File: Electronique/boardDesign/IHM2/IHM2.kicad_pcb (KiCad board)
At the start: 2 copper layers, 12 x 12 mm, 14 parts, among them J1 Conn_01x14, SW1 SW_Push_Dual_INIT, SW2 SW_Push_Dual_START, SW3 SW_Push_Dual_PAUSE, SW4 RotaryEncoder_Switch, U1 ER_OLEDM0.91_1x-I2C

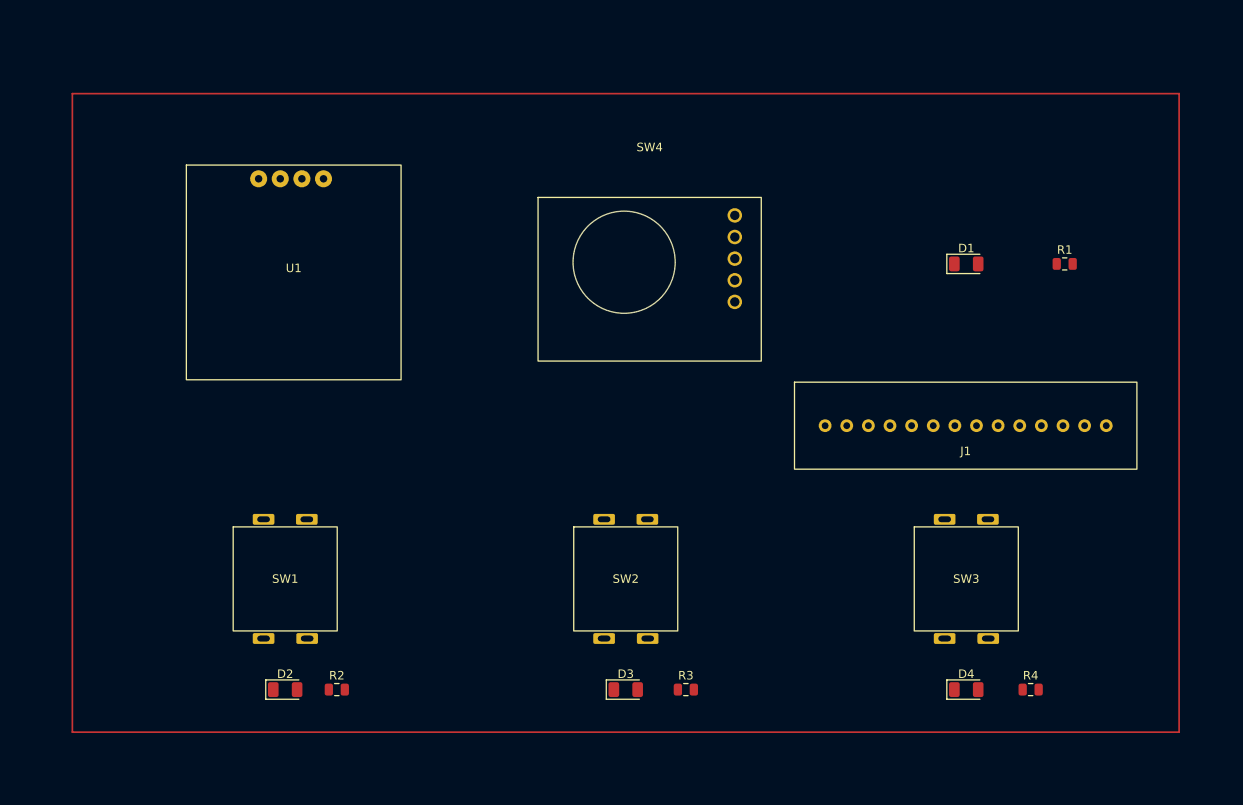
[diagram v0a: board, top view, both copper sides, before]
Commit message: feat : creation of PCB HMI with corresponding schematics and footprints doc : created links list for online resources
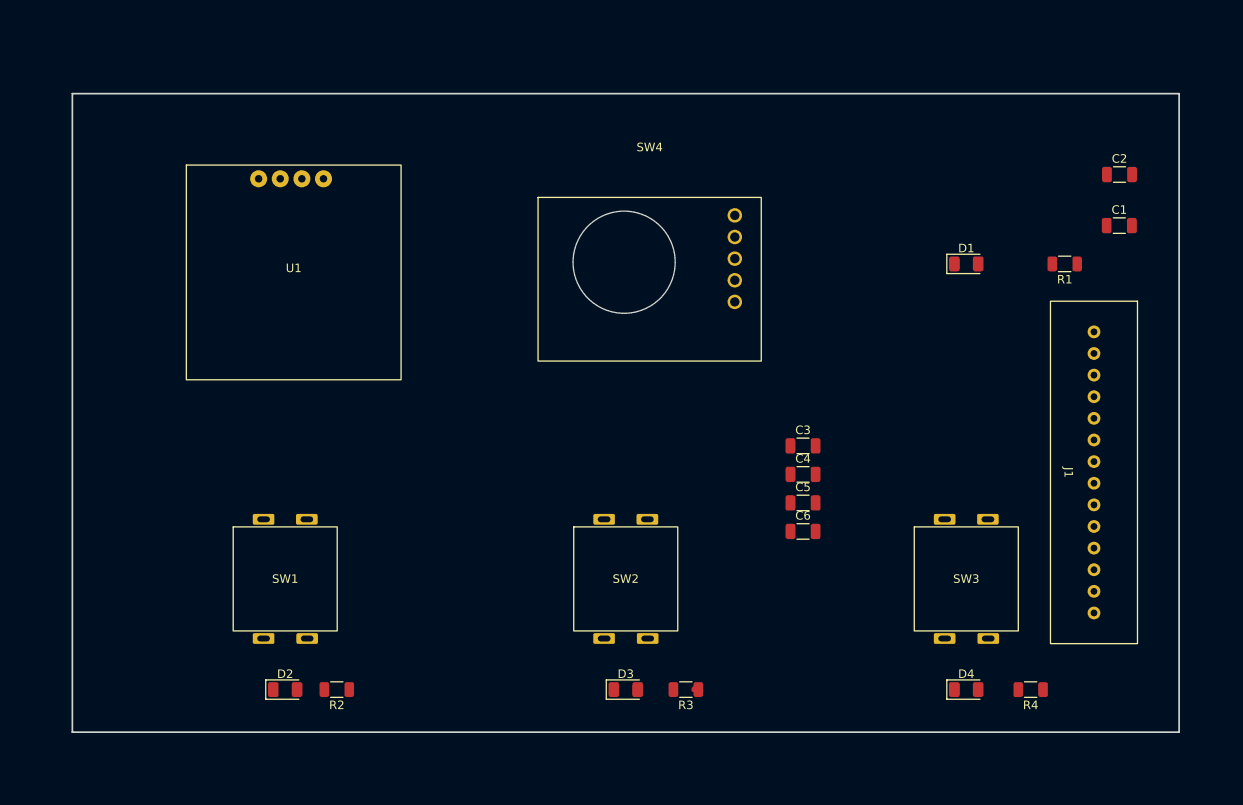
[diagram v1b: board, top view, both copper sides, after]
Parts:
- added C1: 1uF, Capacitor_SMD:C_1206_3216Metric, F.Cu at (188.5, 72.0)
- added C2: 100nF, Capacitor_SMD:C_1206_3216Metric, F.Cu at (188.5, 66.0)
- added C3: 100nF, Capacitor_SMD:C_1206_3216Metric, F.Cu at (151.3, 97.9)
- added C4: 33nF, Capacitor_SMD:C_1206_3216Metric, F.Cu at (151.3, 101.2)
- added C5: 33nF, Capacitor_SMD:C_1206_3216Metric, F.Cu at (151.3, 104.6)
- added C6: 100nF, Capacitor_SMD:C_1206_3216Metric, F.Cu at (151.3, 107.9)
- R1, R2, R3, R4: footprint PCM_4ms_Resistor:R_0805_2012Metric -> Resistor_SMD:R_1206_3216Metric
- moved J1 16.0 mm to (185.5, 101.0), turned to -90 degrees
- turned R1 to 180 degrees
- turned R2 to 180 degrees
- turned R3 to 180 degrees
- turned R4 to 180 degrees
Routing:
- net /LED_START: track 0.00 -> 0.71 mm
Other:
- board size 12 x 12 mm -> 130 x 75 mm

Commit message: fix : added capacitors for power supply and I2C component refactor : removed via rollback : wrong IHM2 version (1 GND layer), recovered feat : added pin description on 1x14 pinset style : added logos
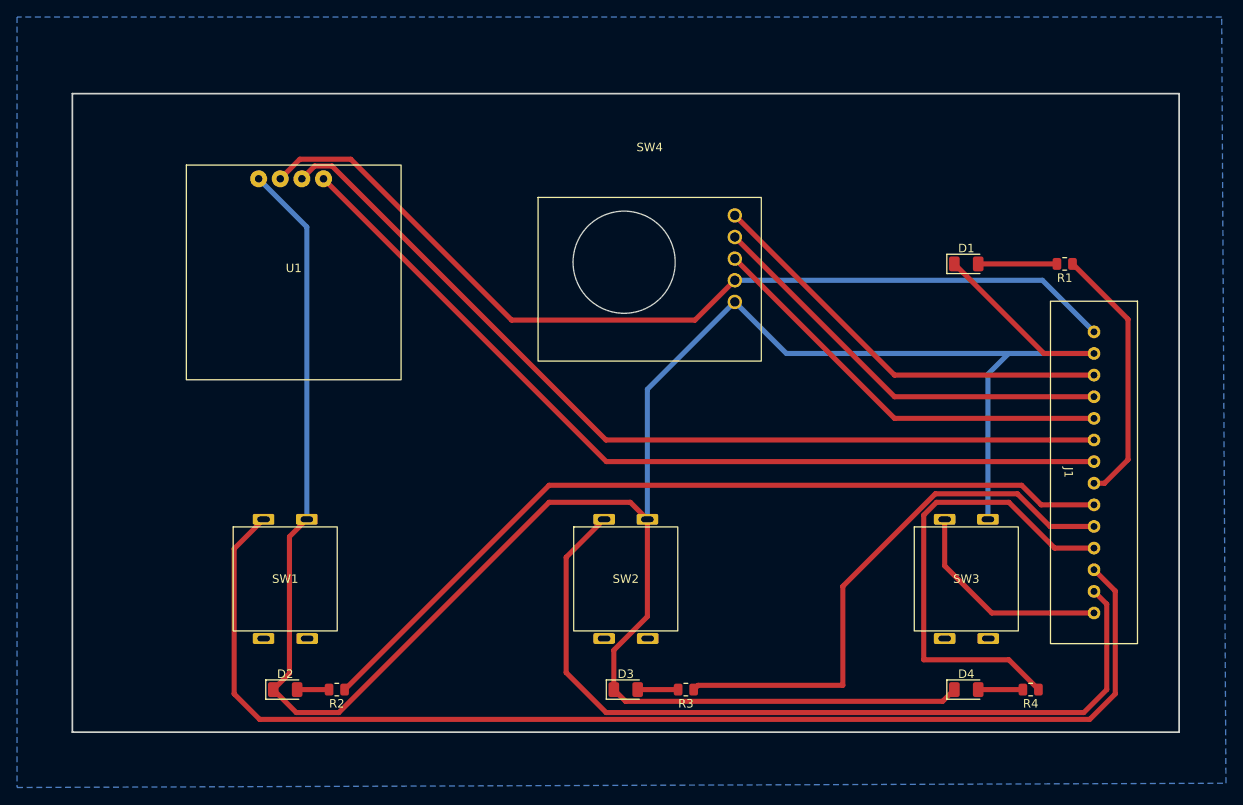
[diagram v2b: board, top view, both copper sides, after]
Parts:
- removed C1: 1uF, Capacitor_SMD:C_1206_3216Metric
- removed C2, C3, C6: 100nF, Capacitor_SMD:C_1206_3216Metric
- removed C4, C5: 33nF, Capacitor_SMD:C_1206_3216Metric
- R1, R2, R3, R4: footprint Resistor_SMD:R_1206_3216Metric -> Resistor_SMD:R_0805_2012Metric
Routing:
- net GND: track 0.00 -> 298.6 mm
- net /SW_INIT_OUT: track 0.00 -> 143.5 mm
- net +5V: track 0.00 -> 108.8 mm
- net /SCL_SCREEN: track 0.00 -> 107.0 mm
- net /SDA_SCREEN: track 0.00 -> 104.3 mm
- net /LED_INIT: track 0.00 -> 98.9 mm
- net /SW_START_OUT: track 0.00 -> 98.6 mm
- net /LED_START: track 0.71 -> 64.9 mm
- net /LED_PAUSE: track 0.00 -> 54.8 mm
- net /SW_ROT: track 0.00 -> 50.0 mm
- net /CLK_ROT: track 0.00 -> 50.0 mm
- net /DT_ROT: track 0.00 -> 50.0 mm
- net /LED_POW: track 0.00 -> 30.8 mm
- net /SW_PAUSE_OUT: track 0.00 -> 25.3 mm
- net Net-(D1-A): track 0.00 -> 9.22 mm
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- added copper zone on B.Cu, net GND
